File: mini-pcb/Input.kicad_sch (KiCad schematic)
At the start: 10 parts, among them U2 OPA1664D, U3 OPA1655DBV

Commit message: almost done with mini pcb
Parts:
- added R13, R14: 100, Resistor_SMD:R_0603_1608Metric, symbol Device:R
- added R15, R17: 10k, Resistor_SMD:R_0603_1608Metric, symbol Device:R
- added R16, R18: 39k, Resistor_SMD:R_0603_1608Metric, symbol Device:R
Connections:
- net AUDIO_IN_JACK_LEFT_BUF: now also R13.2; no longer U2.1, U2.2 (-)
- net AUDIO_IN_JACK_RIGHT_BUF: now also R14.2; no longer U2.6 (-), U2.7
- net AGND renamed GND
- net GND: now also R15.1, R17.1
- new net: R15.2, R16.2, U2.2 (-)
- new net: R13.1, R16.1, U2.1
- new net: R14.1, R18.1, U2.7
- new net: R17.2, R18.2, U2.6 (-)

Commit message: made final touches and bom still needs through testing
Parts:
- added R23, R24: 100k, Resistor_SMD:R_0603_1608Metric, symbol Device:R
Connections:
- net AUDIO_IN_JACK_LEFT: now also R23.2; no longer C6.1, R2.2
- net AUDIO_IN_JACK_RIGHT: now also R24.2; no longer C2.1, R9.2
- new net: C6.1, R2.2, R23.1
- new net: C2.1, R24.1, R9.2
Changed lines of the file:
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@@
 	(wire
 		(pts
-			(xy 194.31 88.9) (xy 195.58 88.9)
+			(xy 182.88 88.9) (xy 184.15 88.9)
 		)
 		(stroke
@@
 	(wire
 		(pts
-			(xy 83.82 86.36) (xy 85.09 86.36)
+			(xy 191.77 88.9) (xy 195.58 88.9)
+		)
+		(stroke
+			(width 0)
+			(type default)
+		)
+	)
+	(wire
+		(pts
+			(xy 66.04 86.36) (xy 71.12 86.36)
 		)
 		(stroke
@@
 		(pts
 			(xy 96.52 86.36) (xy 100.33 86.36)
+		)
+		(stroke
+			(width 0)
+			(type default)
+		)
+	)
+	(wire
+		(pts
+			(xy 78.74 86.36) (xy 85.09 86.36)
 		)
 		(stroke
@@
 	(global_label "AUDIO_IN_JACK_LEFT"
 		(shape input)
-		(at 83.82 86.36 180)
+		(at 66.04 86.36 180)
 		(fields_autoplaced yes)
 		(effects
@@
 		)
 		(property "Intersheetrefs" "${INTERSHEET_REFS}"
-			(at 61.5428 86.36 0)
+			(at 43.7628 86.36 0)
 			(effects
 				(font
@@
 	(global_label "AUDIO_IN_JACK_RIGHT"
 		(shape input)
-		(at 194.31 88.9 180)
+		(at 182.88 88.9 180)
 		(fields_autoplaced yes)
 		(effects
@@
 		)
 		(property "Intersheetrefs" "${INTERSHEET_REFS}"
-			(at 170.8232 88.9 0)
+			(at 159.3932 88.9 0)
 			(effects
 				(font
@@
 	(symbol
 		(lib_id "Device:R")
+		(at 187.96 88.9 270)
+		(unit 1)
+		(exclude_from_sim no)
+		(in_bom yes)
+		(on_board yes)
+		(dnp no)
+		(fields_autoplaced yes)
+		(property "Reference" "R24"
+			(at 187.96 82.55 90)
+			(effects
+				(font
+					(size 1.27 1.27)
+				)
+			)
+		)
+		(property "Value" "100k"
+			(at 187.96 85.09 90)
+			(effects
+				(font
+					(size 1.27 1.27)
+				)
+			)
+		)
+		(property "Footprint" "Resistor_SMD:R_0603_1608Metric"
+			(at 187.96 87.122 90)
+			(effects
+				(font
+					(size 1.27 1.27)
+				)
+				(hide yes)
+			)
+		)
+		(property "Datasheet" "~"
+			(at 187.96 88.9 0)
+			(effects
+				(font
+					(size 1.27 1.27)
+				)
+				(hide yes)
+			)
+		)
+		(property "Description" "Resistor"
+			(at 187.96 88.9 0)
+			(effects
+				(font
+					(size 1.27 1.27)
+				)
+				(hide yes)
+			)
+		)
+		(pin "2"
+		)
+		(pin "1"
+		)
+		(instances
+			(project "mini_pcb"
+				(path "/ac8ee366-0662-41f8-9745-078ec3fbb21b/0ca96f51-23c0-4c17-837f-32f367c7277c"
+					(reference "R24")
+					(unit 1)
+				)
+			)
+		)
+	)
+	(symbol
+		(lib_id "Device:R")
 		(at 100.33 104.14 180)
 		(unit 1)
@@
 					(unit 1)
 				)
+			)
+		)
+	)
+	(symbol
+		(lib_id "Device:R")
+		(at 74.93 86.36 270)
+		(unit 1)
+		(exclude_from_sim no)
+		(in_bom yes)
+		(on_board yes)
+		(dnp no)
+		(fields_autoplaced yes)
+		(property "Reference" "R23"
+			(at 74.93 80.01 90)
+			(effects
+				(font
+					(size 1.27 1.27)
+				)
+			)
+		)
+		(property "Value" "100k"
+			(at 74.93 82.55 90)
+			(effects
+				(font
+					(size 1.27 1.27)
+				)
+			)
+		)
+		(property "Footprint" "Resistor_SMD:R_0603_1608Metric"
+			(at 74.93 84.582 90)
+			(effects
+				(font
+					(size 1.27 1.27)
+				)
+				(hide yes)
+			)
+		)
+		(property "Datasheet" "~"
+			(at 74.93 86.36 0)
+			(effects
+				(font
+					(size 1.27 1.27)
+				)
+				(hide yes)
+			)
+		)
+		(property "Description" "Resistor"
+			(at 74.93 86.36 0)
+			(effects
+				(font
+					(size 1.27 1.27)
+				)
+				(hide yes)
+			)
+		)
+		(pin "2"
+		)
+		(pin "1"
+		)
+		(instances
+			(project "mini_pcb"
+				(path "/ac8ee366-0662-41f8-9745-078ec3fbb21b/0ca96f51-23c0-4c17-837f-32f367c7277c"
+					(reference "R23")
+					(unit 1)
+				)

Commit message: ordered pcb
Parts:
- removed C6: 10uf, Capacitor_SMD:C_0805_2012Metric, symbol Device:C
- removed R10, R2, R6, R7, R9: 1M, Resistor_SMD:R_0603_1608Metric, symbol Device:R
- removed R15, R17: 10k, Resistor_SMD:R_0603_1608Metric, symbol Device:R
- removed R16, R18: 39k, Resistor_SMD:R_0603_1608Metric, symbol Device:R
- removed R23, R24: 100k, Resistor_SMD:R_0603_1608Metric, symbol Device:R
- removed U3: OPA1655DBV, Package_TO_SOT_SMD:SOT-23-5, symbol Amplifier_Operational:OPA1655DBV
- added C13: 1nf, Capacitor_SMD:C_0805_2012Metric, symbol Device:C
- added C14, C15: 10uf, Capacitor_SMD:C_0805_2012Metric, symbol Device:C
- added R3, R4: 100, Resistor_SMD:R_0603_1608Metric, symbol Device:R
- added R5: 1M, Resistor_SMD:R_0603_1608Metric, symbol Device:R
- C2: value 10uf -> 1nf; MPN (none) -> C46653
- R1: MPN (none) -> C22935
- R13, R14: MPN (none) -> C22775
- U2: MPN (none) -> C69414
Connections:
- net +2.5V: now also R5.2
- net AUDIO_IN_JACK_LEFT: now also R3.2
- net AUDIO_IN_JACK_RIGHT: now also R4.2
- net GND: now also C2.1, C13.1
- net at R1.1, U2.3 (+): now also C14.2
- net at U2.2 (-): now also C2.2, R13.1, U2.1
- net at R14.1, U2.7: now also U2.6 (-), C13.2
- net at U2.5 (+): now also C15.2, R5.1; no longer C2.2
- new net: C15.1, R4.1
- new net: C14.1, R3.1

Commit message: made mini-pcb report
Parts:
- added R10, R8: 2M, Resistor_SMD:R_0603_1608Metric, symbol Device:R
- C14, C15: value 10uf -> 47nF; MPN C440198 -> C2182212
- R1, R5: value 1M -> 2M; MPN C22935 -> C22976
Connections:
- net GND: now also R10.1, R8.1
- net at C14.2, R1.1, U2.3 (+): now also R10.2
- net at C15.2, R5.1, U2.5 (+): now also R8.2
- net +2.5V renamed +5V
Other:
- moved on the sheet: C14, C15, R1, R3, R5

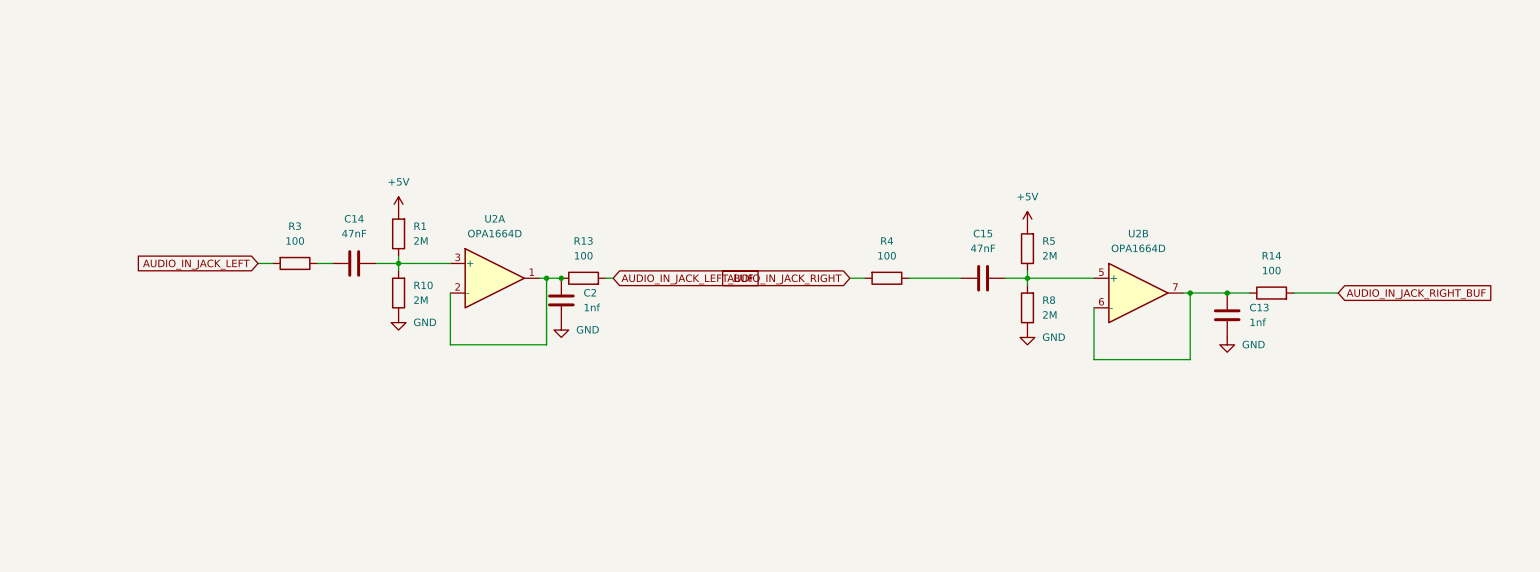
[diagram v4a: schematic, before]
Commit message: I will be re writing the code to use the daisy-embassy library because the Daisy one i have been using has a strange but crush effect when there is just a normal passthrough but the daisy-embassy example works well with my PCB also there was a testing problem earlyer with the PCB and the PCB works fine with no changes
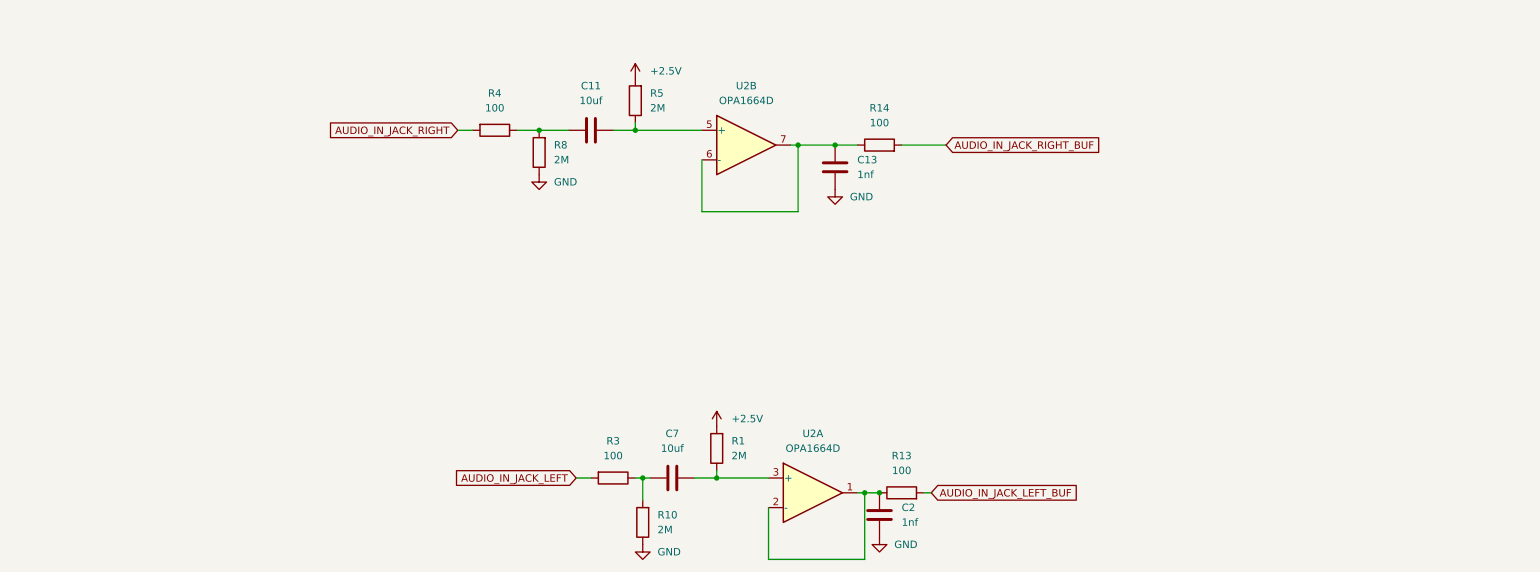
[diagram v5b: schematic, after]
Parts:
- removed C14, C15: 47nF, Capacitor_SMD:C_0805_2012Metric, symbol Device:C
- added C11, C7: 10uf, Capacitor_SMD:C_0805_2012Metric, symbol Device:C
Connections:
- net at R1.1, U2.3 (+): now also C7.2; no longer R10.2
- net at R4.1: now also R8.2, C11.1
- net at R5.1, U2.5 (+): now also C11.2; no longer R8.2
- net at R3.1: now also R10.2, C7.1
- net +5V renamed +2.5V
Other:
- moved on the sheet: C13, C2, R1, R13, R14, R3, R4, R5, U2A, U2B
